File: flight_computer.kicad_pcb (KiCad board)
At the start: 4 copper layers, 95.9 x 90.2 mm, 144 parts, among them J1 436500204, J10 TSW-102-07-F-S, J11 TSW-103-07-F-S, J12 SMA-J-P-H-ST-EM1, J2 0530480210, J3 0530480210, J4 398800302, J5 398800302, J6 398800302, J7 398800302, J8 0530480810, J9 USB4105-GF-A-120, Q6 SI1016CX-T1-GE3, U1 STM32F405VGT7, U10 LT6000IDCB#TRMPBF, U11 NC7WZ07P6X, U12 B39162B4300F210, U13 MS561101BA03-50, U14 IAM-20380HT, U15 H3LIS331DLTR, U2 INA229AQDGSRQ1, U3 TPS62130AQRGTRQ1, U4 TPS62130AQRGTRQ1, U5 S25FL256LAGNFM010, U6 USBLC6-2P6, U7 MMC5983MA, U8 AIS2IHTR, U9 MAX-M10S-00B, Y1 25MHz

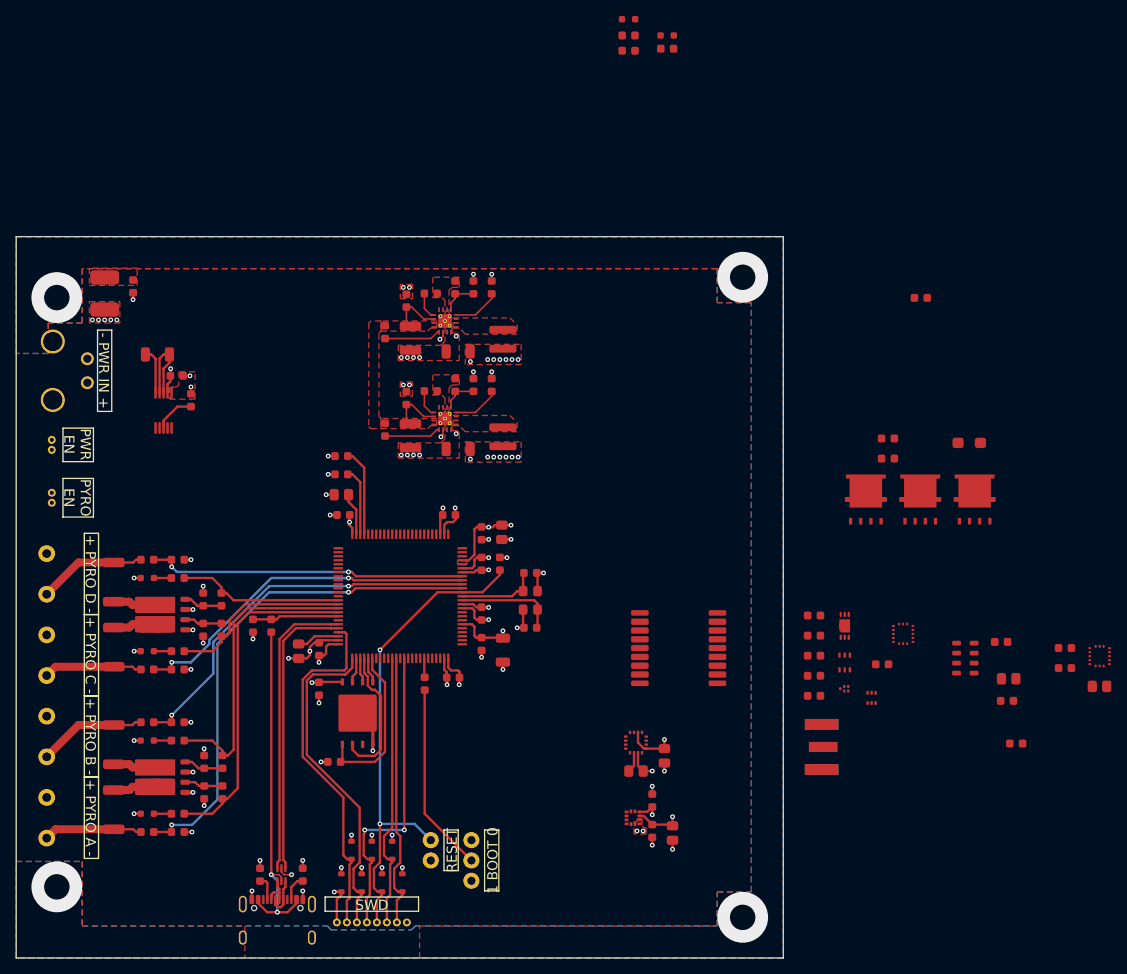
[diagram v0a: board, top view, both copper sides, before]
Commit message: Update to power section
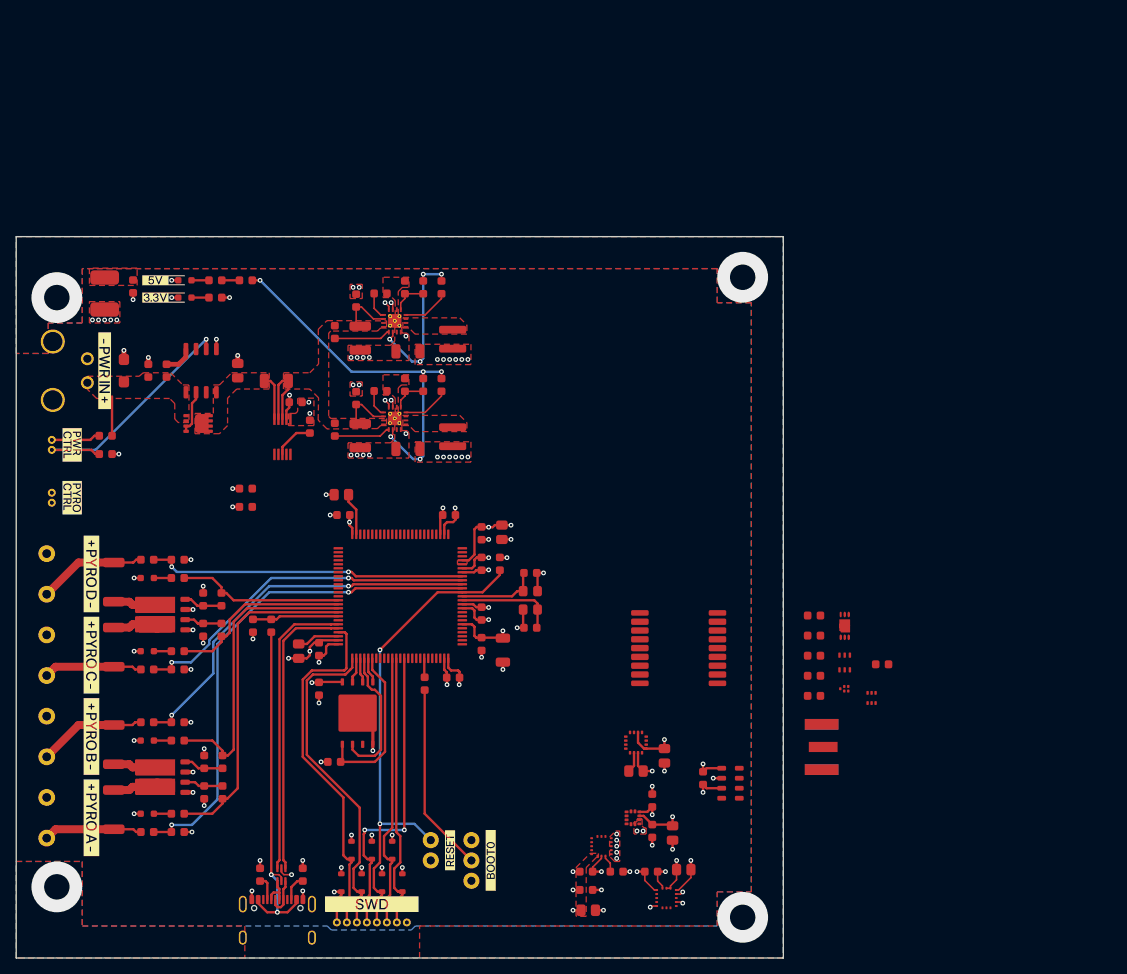
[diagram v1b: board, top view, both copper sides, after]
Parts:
- removed Q1, Q2, Q3: ~, passive_mosfet:SQJ211ELP-T1_GE3
- removed R6: 100kΩ, passive_resistor:R_0603_Density_Nominal
- added C41: 100nF, passive_capacitor:C_0603_Density_Nominal, F.Cu at (121.2, 67.3)
- added C42: 1μF, passive_capacitor:C_0805_Density_Nominal, F.Cu at (132.4, 67.3)
- added C43: 100nF, passive_capacitor:C_0603_Density_Nominal, F.Cu at (123.5, 67.3)
- added Q7: DMT6007LFGQ-7, passive_mosfet:DMT6007LFGQ-7, F.Cu at (127.4, 73.9)
- added U16: LM74700QDRQ1, ic_power:LM74700QDRQ1, F.Cu at (127.8, 67.3)
- added kibuzzard-6A2D86D8: G***, kibuzzard-6A2D86D8, F.Cu at (122.1, 58.1)
- added kibuzzard-6A2D86DB: G***, kibuzzard-6A2D86DB, F.Cu at (122.1, 56.0)
- added kibuzzard-6A2D8804: G***, kibuzzard-6A2D8804, F.Cu at (111.7, 76.6)
- added kibuzzard-6A2D8820: G***, kibuzzard-6A2D8820, F.Cu at (111.7, 83.2)
- added kibuzzard-6A2D888E: G***, kibuzzard-6A2D888E, F.Cu at (114.1, 92.7)
- added kibuzzard-6A2D88AE: G***, kibuzzard-6A2D88AE, F.Cu at (115.8, 67.3)
- added kibuzzard-6A2D88CA: G***, kibuzzard-6A2D88CA, F.Cu at (114.1, 102.8)
- added kibuzzard-6A2D88D0: G***, kibuzzard-6A2D88D0, F.Cu at (114.1, 113.0)
- added kibuzzard-6A2D88D5: G***, kibuzzard-6A2D88D5, F.Cu at (114.1, 123.2)
- added kibuzzard-6A2D89E8: G***, kibuzzard-6A2D89E8, F.Cu at (149.2, 134.0)
- added kibuzzard-6A2D8A19: G***, kibuzzard-6A2D8A19, F.Cu at (158.9, 127.2)
- added kibuzzard-6A2D8A5A: G***, kibuzzard-6A2D8A5A, F.Cu at (164.0, 128.5)
- D1: footprint passive_diode:SZSMF20AT1G -> passive_diode:SZSMF4L17CAT3G
- R2: value 100kΩ -> 10kΩ
- moved D1 106.0 mm to (118.2, 67.3), turned to 90 degrees
- moved R3 97.8 mm to (115.9, 77.7)
- moved R2 97.8 mm to (115.9, 75.4), turned to 180 degrees
- moved D6 68.6 mm to (125.8, 58.1)
- moved R43 64.5 mm to (129.6, 58.1), turned to 180 degrees
- moved D7 64.4 mm to (125.8, 56.0)
- moved U15 62.0 mm to (186.0, 133.2)
- moved C40 61.5 mm to (179.8, 129.9)
- moved R44 60.0 mm to (129.6, 56.0), turned to 180 degrees
- moved C35 60.0 mm to (176.2, 134.7)
- moved C39 58.8 mm to (184.1, 129.9)
- moved C36 57.7 mm to (175.9, 132.2)
- moved C38 56.8 mm to (188.1, 129.6)
- moved C37 56.1 mm to (175.9, 129.9)
- moved R45 55.8 mm to (133.4, 56.0)
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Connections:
- net Net-(U2-IN+) renamed /power/VIN_PROT
- D1 pad 1: Net-(D1-Pad1) -> VIN
- D1 pad 2: Net-(D1-Pad2) -> GND
- J2 pad 2: GND -> Net-(U16-EN)
- J3 pad 1: Net-(J3-Pad1) -> /power/VSENSE
- J3 pad 2: GND -> Net-(J3-Pad2)
- J4 pad 1: Net-(J4-Pad1) -> Net-(J3-Pad2)
- J5 pad 1: Net-(J4-Pad1) -> Net-(J3-Pad2)
- J6 pad 1: Net-(J4-Pad1) -> Net-(J3-Pad2)
- J7 pad 1: Net-(J4-Pad1) -> Net-(J3-Pad2)
- R2 pad 1: Net-(D1-Pad2) -> VIN
- R2 pad 2: GND -> Net-(J2-Pad1)
- R3 pad 1: Net-(D1-Pad1) -> Net-(U16-EN)
- R3 pad 2: Net-(J2-Pad1) -> GND
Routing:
- net +5V: track 2.69 -> 47.0 mm, vias 10 -> 11
- net +3.3V: track 67.9 -> 101.8 mm, vias 29 -> 36
- net Net-(U16-EN): track 0.00 -> 32.4 mm, vias 0 -> 1
- net GND: track 82.1 -> 114.5 mm, vias 74 -> 101
- net I2C2.SCL: track 11.0 -> 0.00 mm
- net I2C2.SDA: track 8.49 -> 0.00 mm
- net Net-(J2-Pad1): track 0.00 -> 6.15 mm
- net Net-(U16-GATE): track 0.00 -> 5.64 mm
- net VIN: track 0.00 -> 4.91 mm
- net /power/VCAP: track 0.00 -> 3.78 mm
- net Net-(R44-Pad1): track 0.00 -> 2.21 mm
- net /sensors/GYRO_REGOUT: track 0.00 -> 2.20 mm
- net Net-(D7-Pad2): track 0.00 -> 2.19 mm
- net Net-(D6-Pad2): track 0.00 -> 2.19 mm
- added copper zone on F.Cu, net /power/+3.3V_SW
- added copper zone on F.Cu, net /power/+5V_SW
- added copper zone on F.Cu, net /power/VIN_PROT
- added copper zone on F.Cu, net /power/VSENSE
- added copper zone on F.Cu, net VIN
- removed copper zone on F.Cu, net (none)
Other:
- board text removed: "+ PYRO A -"
- board text removed: "+ PYRO B -"
- board text removed: "+ PYRO C -"
- board text removed: "+ PYRO D -"
- board text removed: "- PWR IN +"
- board text removed: "1 BOOT 0"
- board text removed: "PWR EN"
- board text removed: "PYRO EN"
- board text removed: "RESET"
- board text removed: "SWD"

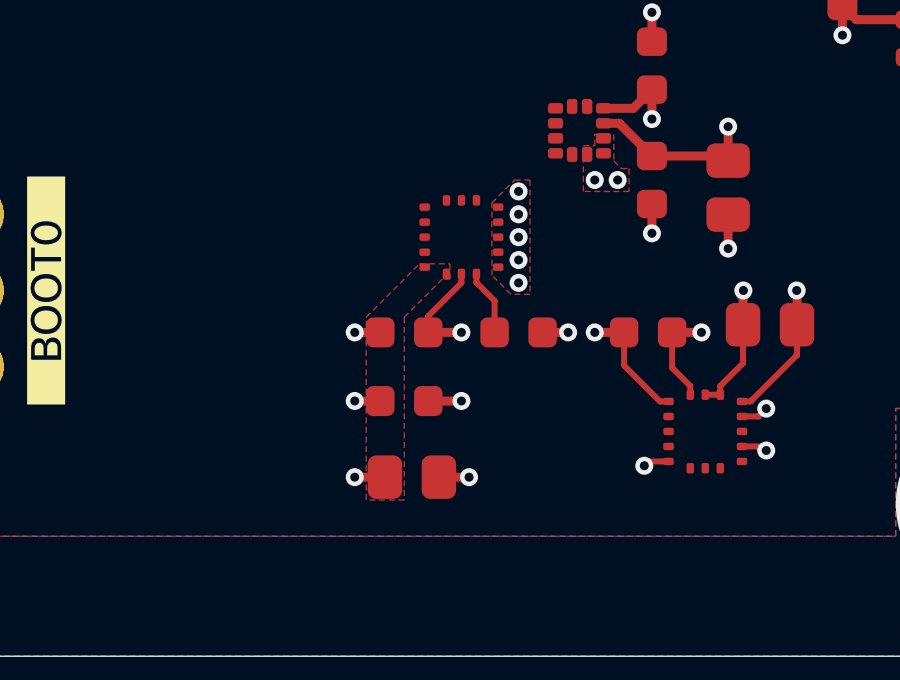
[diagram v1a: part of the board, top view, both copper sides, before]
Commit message: Move component to test workflows
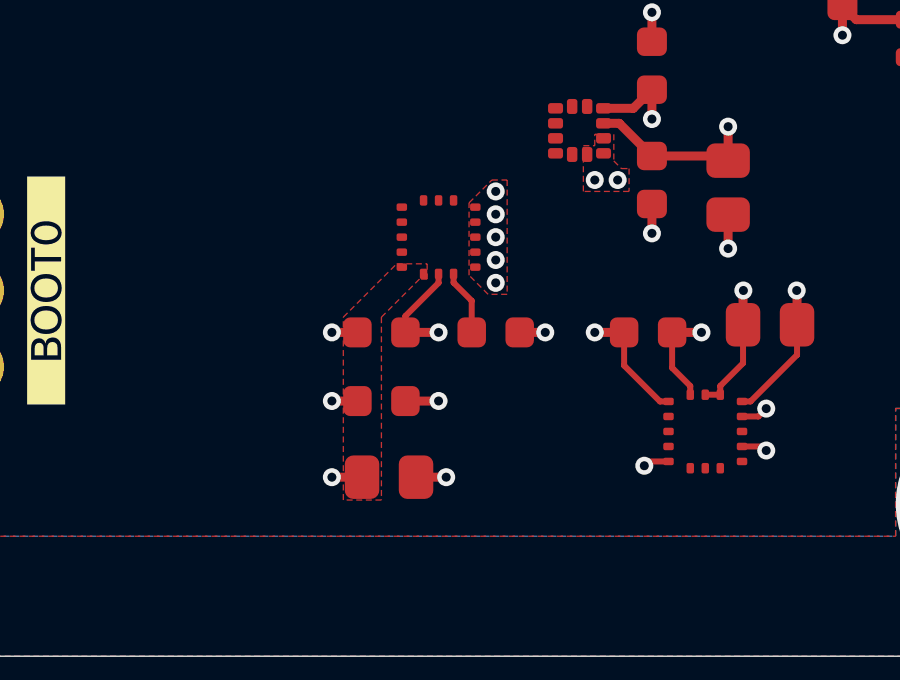
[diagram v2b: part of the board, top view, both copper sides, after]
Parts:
- moved C35 0.76 mm to (175.4, 134.7)
- moved C36 0.76 mm to (175.2, 132.2)
- moved C37 0.76 mm to (175.2, 129.9)
- moved C40 0.76 mm to (179.0, 129.9)
- moved U14 0.76 mm to (177.1, 126.7)
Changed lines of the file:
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@@
 	(footprint "passive_capacitor:C_0805_Density_Nominal"
 		(layer "F.Cu")
-		(at 176.202 134.725)
+		(at 175.44 134.725)
 		(descr "SMD Capacitor 0805 Density Level B (Nominal)")
 		(property "Reference" "C35"
@@
 	(footprint "passive_capacitor:C_0603_Density_Nominal"
 		(layer "F.Cu")
-		(at 179.758 129.899)
+		(at 178.996 129.899)
 		(descr "SMD Capacitor 0603 Density Level B (Nominal)")
 		(property "Reference" "C40"
@@
 	(footprint "ic_sensor:IAM-20380HT"
 		(layer "F.Cu")
-		(at 177.853 126.724)
+		(at 177.091 126.724)
 		(property "Reference" "U14"
 			(at 0 -0.5 0)
@@
 	(footprint "passive_capacitor:C_0603_Density_Nominal"
 		(layer "F.Cu")
-		(at 175.948 132.187997)
+		(at 175.186 132.187997)
 		(descr "SMD Capacitor 0603 Density Level B (Nominal)")
 		(property "Reference" "C36"
@@
 	(footprint "passive_capacitor:C_0603_Density_Nominal"
 		(layer "F.Cu")
-		(at 175.948 129.899)
+		(at 175.186 129.899)
 		(descr "SMD Capacitor 0603 Density Level B (Nominal)")
 		(property "Reference" "C37"
@@
 	)
 	(segment
-		(start 176.748 129.899)
-		(end 176.748 129.353)
+		(start 175.986 129.899)
+		(end 175.986 129.353)
 		(width 0.2)
 		(layer "F.Cu")
@@
 	)
 	(segment
-		(start 177.853 128.248)
-		(end 177.853 127.949)
+		(start 177.091 128.248)
+		(end 177.091 127.949)
 		(width 0.2)
 		(layer "F.Cu")
@@
 	)
 	(segment
-		(start 180.558 129.899)
-		(end 181.409 129.899)
+		(start 179.796 129.899)
+		(end 180.647 129.899)
 		(width 0.3)
 		(layer "F.Cu")
@@
 	)
 	(segment
-		(start 178.107 134.725)
-		(end 177.102 134.725)
+		(start 177.345 134.725)
+		(end 176.34 134.725)
 		(width 0.3)
 		(layer "F.Cu")
@@
 	)
 	(segment
-		(start 177.850003 132.187997)
-		(end 176.748 132.187997)
+		(start 177.088003 132.187997)
+		(end 175.986 132.187997)
 		(width 0.3)
 		(layer "F.Cu")
@@
 	)
 	(segment
-		(start 177.853 132.185)
-		(end 177.850003 132.187997)
+		(start 177.091 132.185)
+		(end 177.088003 132.187997)
 		(width 0.3)
 		(layer "F.Cu")
@@
 	)
 	(segment
-		(start 176.748 129.353)
-		(end 177.853 128.248)
+		(start 175.986 129.353)
+		(end 177.091 128.248)
 		(width 0.2)
 		(layer "F.Cu")
@@
 	)
 	(segment
-		(start 177.853 129.899)
-		(end 176.748 129.899)
+		(start 177.091 129.899)
+		(end 175.986 129.899)
 		(width 0.3)
 		(layer "F.Cu")
@@
 	)
 	(via
-		(at 179.758 125.2)
+		(at 178.996 125.2)
 		(size 0.6)
 		(drill 0.3)
@@
 	)
 	(via
-		(at 181.409 129.899)
+		(at 180.647 129.899)
 		(size 0.6)
 		(drill 0.3)
@@
 	)
 	(via
-		(at 177.853 129.899)
+		(at 177.091 129.899)
 		(size 0.6)
 		(drill 0.3)
@@
 	)
 	(via
-		(at 179.758 128.248)
+		(at 178.996 128.248)
 		(size 0.6)
 		(drill 0.3)
@@
 	)
 	(via
-		(at 178.107 134.725)
+		(at 177.345 134.725)
 		(size 0.6)
 		(drill 0.3)
@@
 	)
 	(via
-		(at 179.758 126.724)
+		(at 178.996 126.724)
 		(size 0.6)
 		(drill 0.3)
@@
 	)
 	(via
-		(at 179.758 127.486)
+		(at 178.996 127.486)
 		(size 0.6)
 		(drill 0.3)
@@
 	)
 	(via
-		(at 179.758 125.962)
+		(at 178.996 125.962)
 		(size 0.6)
 		(drill 0.3)
@@
 	)
 	(via
-		(at 177.853 132.185)
+		(at 177.091 132.185)
 		(size 0.6)
 		(drill 0.3)
@@
 	)
 	(segment
-		(start 175.302 134.725)
-		(end 174.297 134.725)
+		(start 174.54 134.725)
+		(end 173.535 134.725)
 		(width 0.3)
 		(layer "F.Cu")
@@
 	)
 	(segment
-		(start 175.148 129.899)
-		(end 174.297 129.899)
+		(start 174.386 129.899)
+		(end 173.535 129.899)
 		(width 0.3)
 		(layer "F.Cu")
@@
 	)
 	(segment
-		(start 174.299997 132.187997)
-		(end 174.297 132.185)
+		(start 173.537997 132.187997)
+		(end 173.535 132.185)
 		(width 0.3)
 		(layer "F.Cu")
@@
 	)
 	(segment
-		(start 175.148 132.187997)
-		(end 174.299997 132.187997)
+		(start 174.386 132.187997)
+		(end 173.537997 132.187997)
 		(width 0.3)
 		(layer "F.Cu")
@@
 	)
 	(via
-		(at 174.297 129.899)
+		(at 173.535 129.899)
 		(size 0.6)
 		(drill 0.3)
@@
 	)
 	(via
-		(at 174.297 134.725)
+		(at 173.535 134.725)
 		(size 0.6)
 		(drill 0.3)
@@
 	)
 	(via
-		(at 174.297 132.185)
+		(at 173.535 132.185)
 		(size 0.6)
 		(drill 0.3)
@@
 	)
 	(segment
-		(start 178.353 128.24)
-		(end 178.958 128.845)
+		(start 177.591 128.24)
+		(end 178.196 128.845)
 		(width 0.2)
 		(layer "F.Cu")
@@
 	)
 	(segment
-		(start 178.353 127.949)
-		(end 178.353 128.24)
+		(start 177.591 127.949)
+		(end 177.591 128.24)
 		(width 0.2)
 		(layer "F.Cu")
@@
 	)
 	(segment
-		(start 178.958 128.845)
-		(end 178.958 129.899)
+		(start 178.196 128.845)
+		(end 178.196 129.899)
 		(width 0.2)
 		(layer "F.Cu")
@@
 		(polygon
 			(pts
-				(xy 176.456 127.613) (xy 177.472 127.613) (xy 177.472 128.121) (xy 177.218 128.121) (xy 175.948 129.391)
-				(xy 175.948 135.487) (xy 174.678 135.487) (xy 174.678 129.391)
+				(xy 175.694 127.613) (xy 176.71 127.613) (xy 176.71 128.121) (xy 176.456 128.121) (xy 175.186 129.391)
+				(xy 175.186 135.487) (xy 173.916 135.487) (xy 173.916 129.391)
 			)
 		)
@@
 		(polygon
 			(pts
-				(xy 180.139 128.629) (xy 179.504 128.629) (xy 178.869 127.994) (xy 178.869 125.581) (xy 179.631 124.819)
-				(xy 180.139 124.819)
+				(xy 179.377 128.629) (xy 178.742 128.629) (xy 178.107 127.994) (xy 178.107 125.581) (xy 178.869 124.819)
+				(xy 179.377 124.819)
 			)
 		)

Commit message: Add README
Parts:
- removed kibuzzard-6A2D8A5A: G***, kibuzzard-6A2D8A5A
- added kibuzzard-6A2DBB13: G***, kibuzzard-6A2DBB13, F.Cu at (164.0, 128.5)
- moved R25 17.6 mm to (150.9, 83.3), turned to -90 degrees
- moved R26 15.3 mm to (148.6, 83.3), turned to -90 degrees
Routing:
- net SPI1.MOSI: track 0.00 -> 32.9 mm, vias 0 -> 2
- net SPI1.MISO: track 0.00 -> 32.4 mm, vias 0 -> 2
- net SPI1.SCLK: track 0.00 -> 32.1 mm
- net I2C2.SCL: track 0.00 -> 5.59 mm
- net I2C2.SDA: track 0.00 -> 4.03 mm
